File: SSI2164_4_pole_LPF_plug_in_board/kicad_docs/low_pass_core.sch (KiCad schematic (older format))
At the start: 31 parts, among them Q1 MMBT3904, Q2 MMBT3906, U1 SSM2164, U2 TL072, U3 TL072

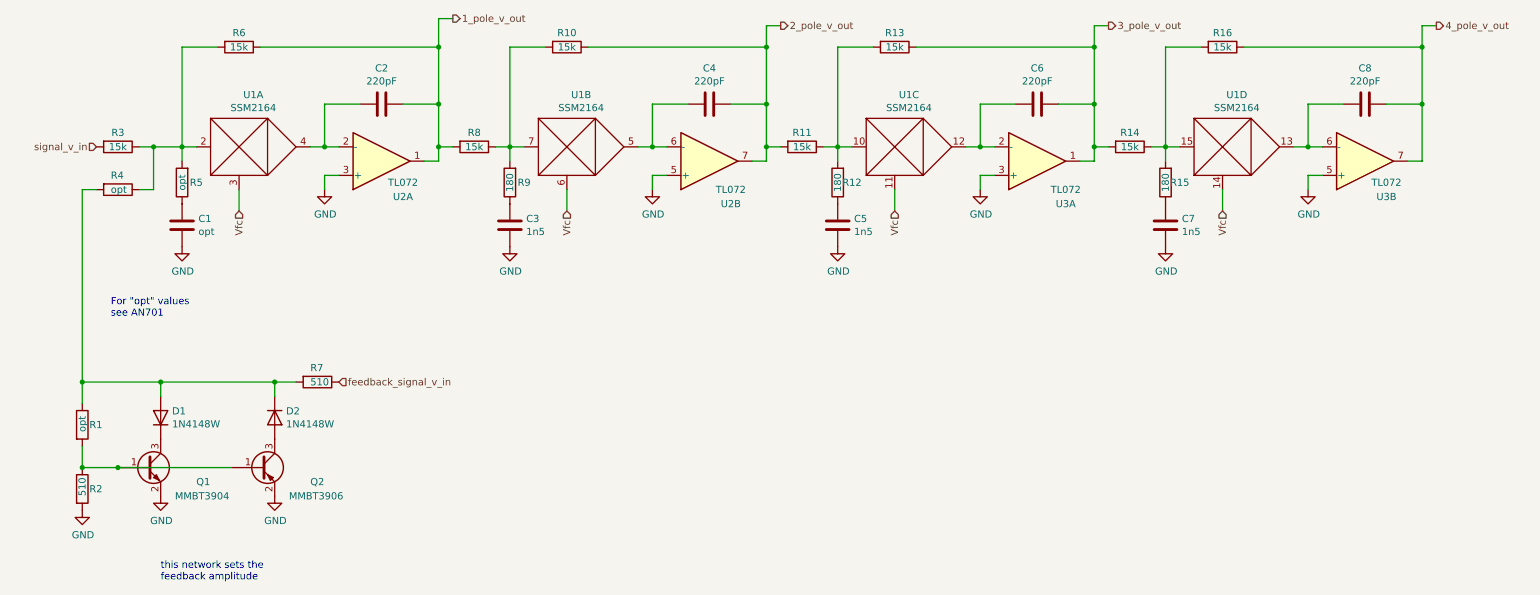
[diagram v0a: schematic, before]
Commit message: progress on SSI2164 LPF
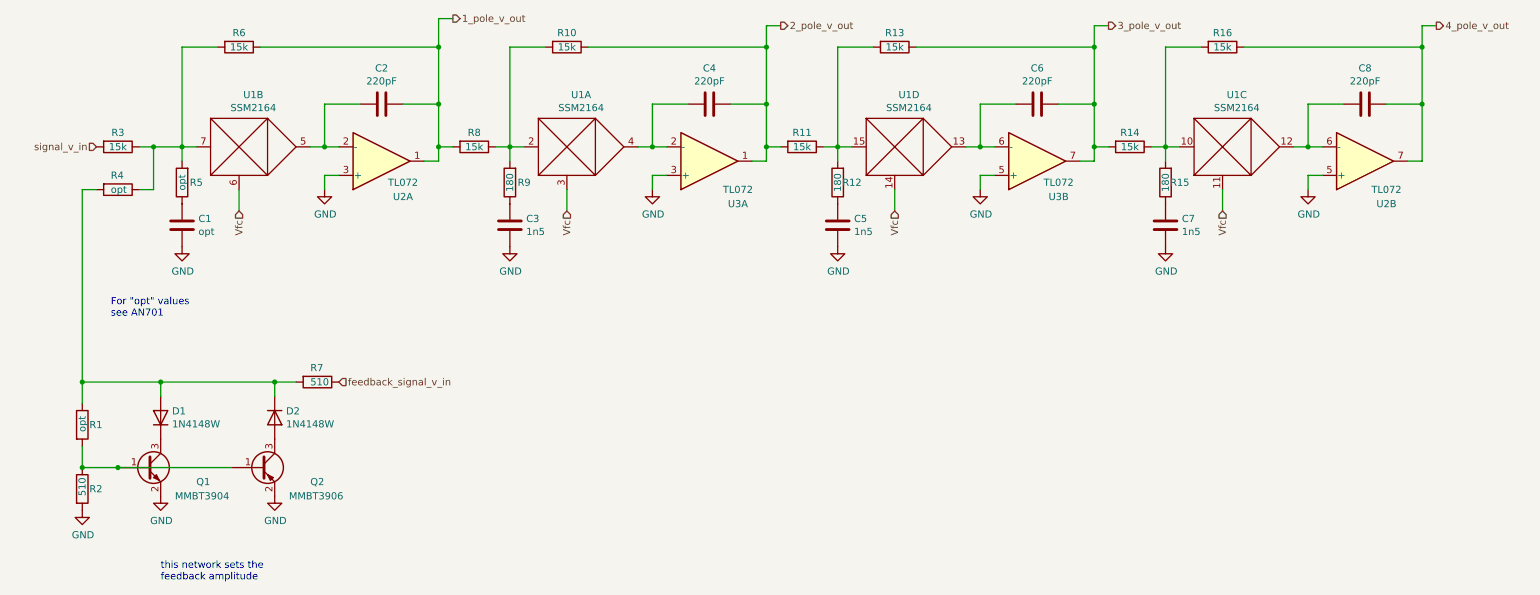
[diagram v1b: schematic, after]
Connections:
- net 2_pole_v_out: now also U3.1; no longer U2.7
- net 3_pole_v_out: now also U3.7; no longer U3.1
- net 4_pole_v_out: now also U2.7; no longer U3.7
- net at R3.1, R4.1, R5.2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: now also U1.7; no longer U1.2
- net at C2.2, U2.2 (-): now also U1.5; no longer U1.4
- net at R10.2, R8.1, R9.2: now also U1.2; no longer U1.7
- net at R11.1, R12.2, R13.2: now also U1.15; no longer U1.10
- net at U1.13, U3.6 (-): now also C6.2; no longer C8.2
- net at R14.1, R15.2, R16.2: now also U1.10; no longer U1.15
- new net: C4.2, U1.4, U3.2 (-)
- new net: C8.2, U1.12, U2.6 (-)
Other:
- moved on the sheet: U1A, U1B, U1C, U1D, U2B, U3A, U3B
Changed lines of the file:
@@
 L lpf_parts:SSM2164 U?
 U 1 1 5F03FD0F
-P 2000 3600
+P 4300 3600
 AR Path="/5EE91CC9/5F03FD0F" Ref="U?"  Part="1"
 AR Path="/5F03FD0F" Ref="U?"  Part="1"
 AR Path="/5EFF89D4/5F03FD0F" Ref="U1"  Part="1"
-F 0 "U1" H 2100 3965 50  0000 C CNN
-F 1 "SSM2164" H 2100 3874 50  0000 C CNN
-F 2 "Package_SO:SOIC-16_3.9x9.9mm_P1.27mm" H 2100 3800 50  0001 C CNN
-F 3 "" H 2100 3800 50  0001 C CNN
-	1    2000 3600
+F 0 "U1" H 4400 3965 50  0000 C CNN
+F 1 "SSM2164" H 4400 3874 50  0000 C CNN
+F 2 "Package_SO:SOIC-16_3.9x9.9mm_P1.27mm" H 4400 3800 50  0001 C CNN
+F 3 "" H 4400 3800 50  0001 C CNN
+	1    4300 3600
 	1    0    0    -1
 $EndComp
@@
 L lpf_parts:SSM2164 U?
 U 2 1 5F03FD3F
-P 4300 3600
+P 2000 3600
 AR Path="/5EE91CC9/5F03FD3F" Ref="U?"  Part="2"
 AR Path="/5F03FD3F" Ref="U?"  Part="2"
 AR Path="/5EFF89D4/5F03FD3F" Ref="U1"  Part="2"
-F 0 "U1" H 4400 3965 50  0000 C CNN
-F 1 "SSM2164" H 4400 3874 50  0000 C CNN
-F 2 "Package_SO:SOIC-16_3.9x9.9mm_P1.27mm" H 4400 3800 50  0001 C CNN
-F 3 "" H 4400 3800 50  0001 C CNN
-	2    4300 3600
+F 0 "U1" H 2100 3965 50  0000 C CNN
+F 1 "SSM2164" H 2100 3874 50  0000 C CNN
+F 2 "Package_SO:SOIC-16_3.9x9.9mm_P1.27mm" H 2100 3800 50  0001 C CNN
+F 3 "" H 2100 3800 50  0001 C CNN
+	2    2000 3600
 	1    0    0    -1
 $EndComp
@@
 L lpf_parts:SSM2164 U?
 U 3 1 5F03FD84
-P 6600 3600
+P 8900 3600
 AR Path="/5EE91CC9/5F03FD84" Ref="U?"  Part="3"
 AR Path="/5F03FD84" Ref="U?"  Part="3"
 AR Path="/5EFF89D4/5F03FD84" Ref="U1"  Part="3"
-F 0 "U1" H 6700 3965 50  0000 C CNN
-F 1 "SSM2164" H 6700 3874 50  0000 C CNN
-F 2 "Package_SO:SOIC-16_3.9x9.9mm_P1.27mm" H 6700 3800 50  0001 C CNN
-F 3 "" H 6700 3800 50  0001 C CNN
-	3    6600 3600
+F 0 "U1" H 9000 3965 50  0000 C CNN
+F 1 "SSM2164" H 9000 3874 50  0000 C CNN
+F 2 "Package_SO:SOIC-16_3.9x9.9mm_P1.27mm" H 9000 3800 50  0001 C CNN
+F 3 "" H 9000 3800 50  0001 C CNN
+	3    8900 3600
 	1    0    0    -1
 $EndComp
@@
 L lpf_parts:SSM2164 U?
 U 4 1 5F03FDC6
-P 8900 3600
+P 6600 3600
 AR Path="/5EE91CC9/5F03FDC6" Ref="U?"  Part="4"
 AR Path="/5F03FDC6" Ref="U?"  Part="4"
 AR Path="/5EFF89D4/5F03FDC6" Ref="U1"  Part="4"
-F 0 "U1" H 9000 3965 50  0000 C CNN
-F 1 "SSM2164" H 9000 3874 50  0000 C CNN
-F 2 "Package_SO:SOIC-16_3.9x9.9mm_P1.27mm" H 9000 3800 50  0001 C CNN
-F 3 "" H 9000 3800 50  0001 C CNN
-	4    8900 3600
+F 0 "U1" H 6700 3965 50  0000 C CNN
+F 1 "SSM2164" H 6700 3874 50  0000 C CNN
+F 2 "Package_SO:SOIC-16_3.9x9.9mm_P1.27mm" H 6700 3800 50  0001 C CNN
+F 3 "" H 6700 3800 50  0001 C CNN
+	4    6600 3600
 	1    0    0    -1
 $EndComp
@@
 L Amplifier_Operational:TL072 U?
 U 2 1 5F03FE1F
-P 5300 3700
+P 9900 3700
 AR Path="/5EE91CC9/5F03FE1F" Ref="U?"  Part="2"
 AR Path="/5F03FE1F" Ref="U?"  Part="2"
 AR Path="/5EFF89D4/5F03FE1F" Ref="U2"  Part="2"
-F 0 "U2" H 5450 4000 50  0000 C CNN
-F 1 "TL072" H 5450 3900 50  0000 C CNN
-F 2 "Package_SO:SOIC-8_3.9x4.9mm_P1.27mm" H 5300 3700 50  0001 C CNN
-F 3 "http://www.ti.com/lit/ds/symlink/tl071.pdf" H 5300 3700 50  0001 C CNN
-	2    5300 3700
-	1    0    0    1
-$EndComp
-$Comp
-L Amplifier_Operational:TL072 U?
-U 1 1 5F03FE25
-P 7600 3700
-AR Path="/5EE91CC9/5F03FE25" Ref="U?"  Part="1"
-AR Path="/5F03FE25" Ref="U?"  Part="1"
-AR Path="/5EFF89D4/5F03FE25" Ref="U3"  Part="1"
-F 0 "U3" H 7800 4000 50  0000 C CNN
-F 1 "TL072" H 7800 3900 50  0000 C CNN
-F 2 "Package_SO:SOIC-8_3.9x4.9mm_P1.27mm" H 7600 3700 50  0001 C CNN
-F 3 "http://www.ti.com/lit/ds/symlink/tl071.pdf" H 7600 3700 50  0001 C CNN
-	1    7600 3700
-	1    0    0    1
-$EndComp
-$Comp
-L Amplifier_Operational:TL072 U?
-U 2 1 5F03FE2B
-P 9900 3700
-AR Path="/5EE91CC9/5F03FE2B" Ref="U?"  Part="2"
-AR Path="/5F03FE2B" Ref="U?"  Part="2"
-AR Path="/5EFF89D4/5F03FE2B" Ref="U3"  Part="2"
-F 0 "U3" H 10050 3950 50  0000 C CNN
-F 1 "TL072" H 10050 3850 50  0000 C CNN
+F 0 "U2" H 10050 4000 50  0000 C CNN
+F 1 "TL072" H 10050 3900 50  0000 C CNN
 F 2 "Package_SO:SOIC-8_3.9x4.9mm_P1.27mm" H 9900 3700 50  0001 C CNN
 F 3 "http://www.ti.com/lit/ds/symlink/tl071.pdf" H 9900 3700 50  0001 C CNN
@@
 	1    0    0    1
 $EndComp
+$Comp
+L Amplifier_Operational:TL072 U?
+U 1 1 5F03FE25
+P 5300 3700
+AR Path="/5EE91CC9/5F03FE25" Ref="U?"  Part="1"
+AR Path="/5F03FE25" Ref="U?"  Part="1"
+AR Path="/5EFF89D4/5F03FE25" Ref="U3"  Part="1"
+F 0 "U3" H 5500 4000 50  0000 C CNN
+F 1 "TL072" H 5500 3900 50  0000 C CNN
+F 2 "Package_SO:SOIC-8_3.9x4.9mm_P1.27mm" H 5300 3700 50  0001 C CNN
+F 3 "http://www.ti.com/lit/ds/symlink/tl071.pdf" H 5300 3700 50  0001 C CNN
+	1    5300 3700
+	1    0    0    1
+$EndComp
+$Comp
+L Amplifier_Operational:TL072 U?
+U 2 1 5F03FE2B
+P 7600 3700
+AR Path="/5EE91CC9/5F03FE2B" Ref="U?"  Part="2"
+AR Path="/5F03FE2B" Ref="U?"  Part="2"
+AR Path="/5EFF89D4/5F03FE2B" Ref="U3"  Part="2"
+F 0 "U3" H 7750 3950 50  0000 C CNN
+F 1 "TL072" H 7750 3850 50  0000 C CNN
+F 2 "Package_SO:SOIC-8_3.9x4.9mm_P1.27mm" H 7600 3700 50  0001 C CNN
+F 3 "http://www.ti.com/lit/ds/symlink/tl071.pdf" H 7600 3700 50  0001 C CNN
+	2    7600 3700
+	1    0    0    1
+$EndComp
